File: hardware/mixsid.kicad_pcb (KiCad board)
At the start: 2 copper layers, 61 x 55.9 mm, 69 parts, among them P1 INPUT, P2 CONTROL, P4 SOCKET LEFT, P5 OUTPUT, P6 SOCKET RIGHT, Q1 BC547, Q2 BC547, U1 GAL16V8, U2 SID2, U3 7812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

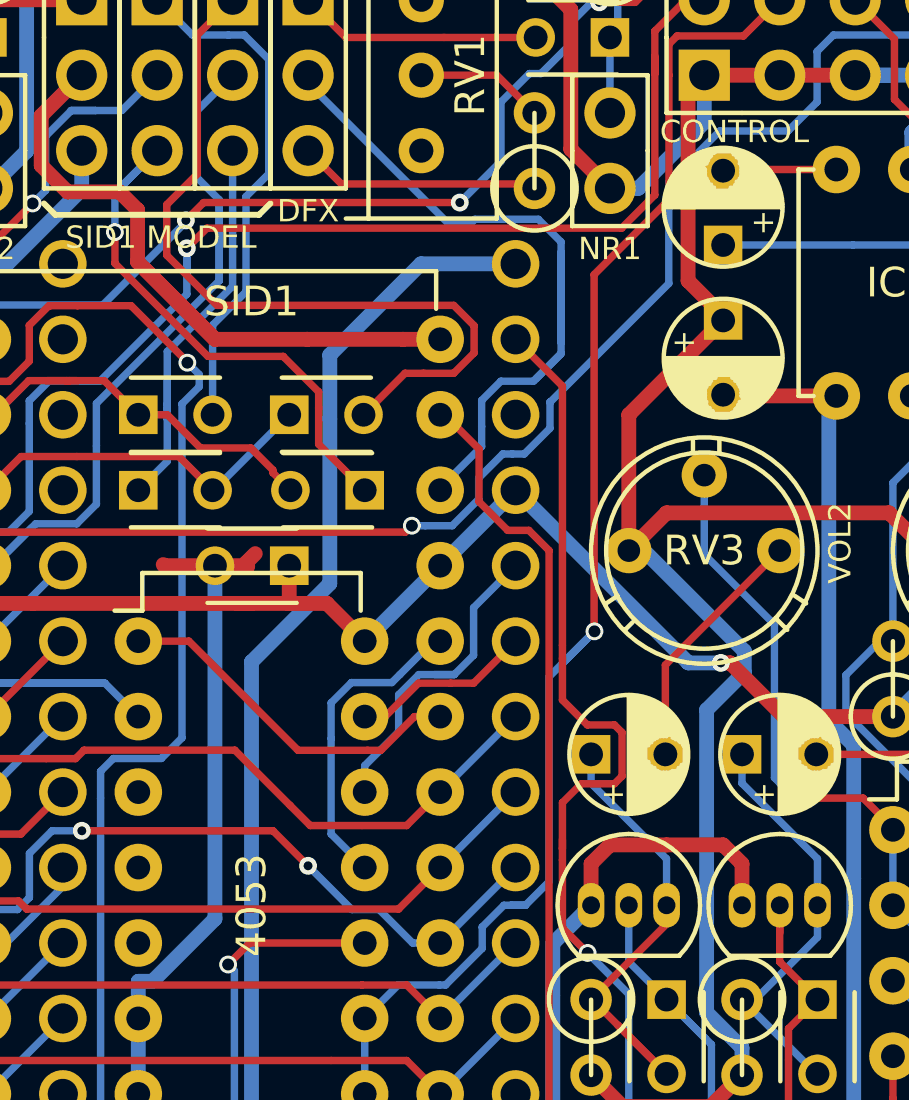
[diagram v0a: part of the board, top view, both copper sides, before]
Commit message: Hardware: Added pin header to access raw audio out as well
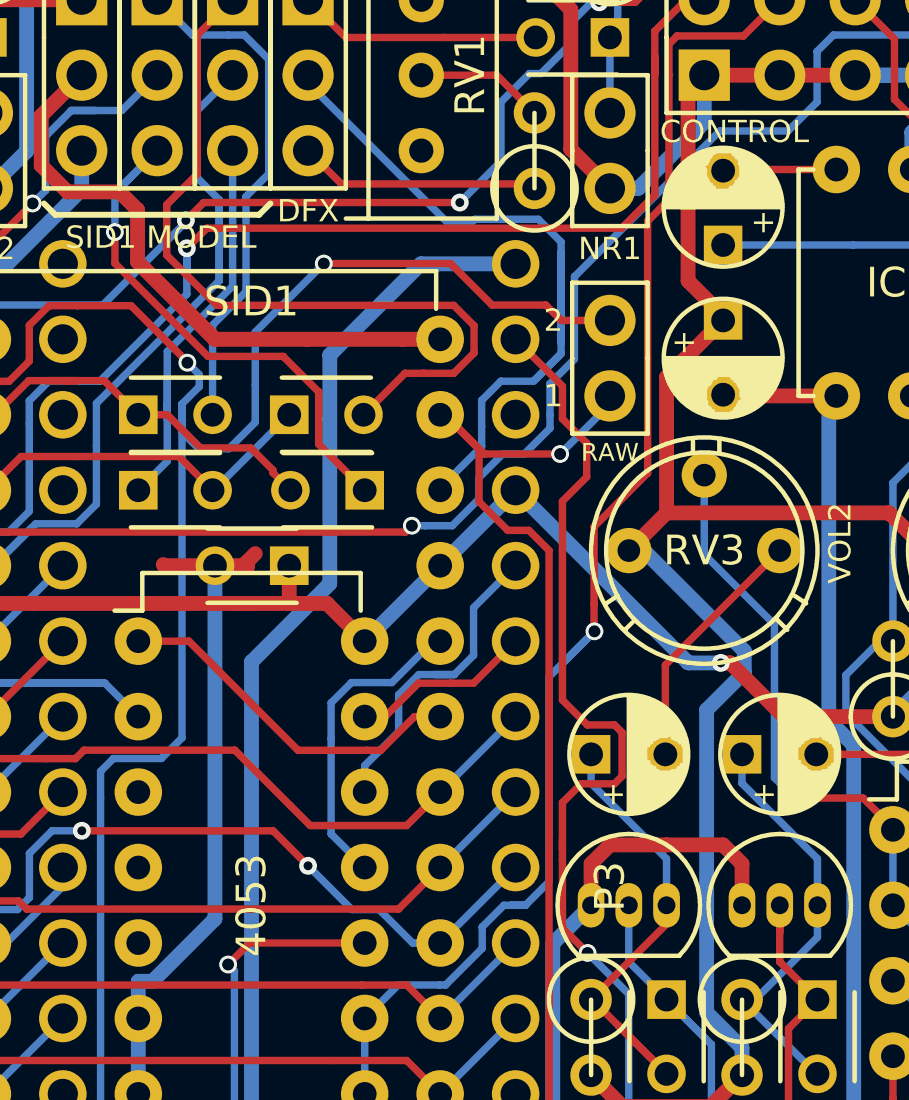
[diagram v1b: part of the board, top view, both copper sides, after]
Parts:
- added P3: RAW, Pinheaders:Pin_Header_Straight_1x02, F.Cu at (169.5, 80.6)
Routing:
- net /S2OUT: track 68.2 -> 88.9 mm, vias 2 -> 3
- net /S1OUT: track 40.4 -> 47.7 mm, vias 0 -> 1
- net GND: track 299.8 -> 298.0 mm
- net /MONO_OUT: track 43.8 -> 44.5 mm
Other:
- board text added: "1"
- board text added: "2"
- board text added: "RAW"

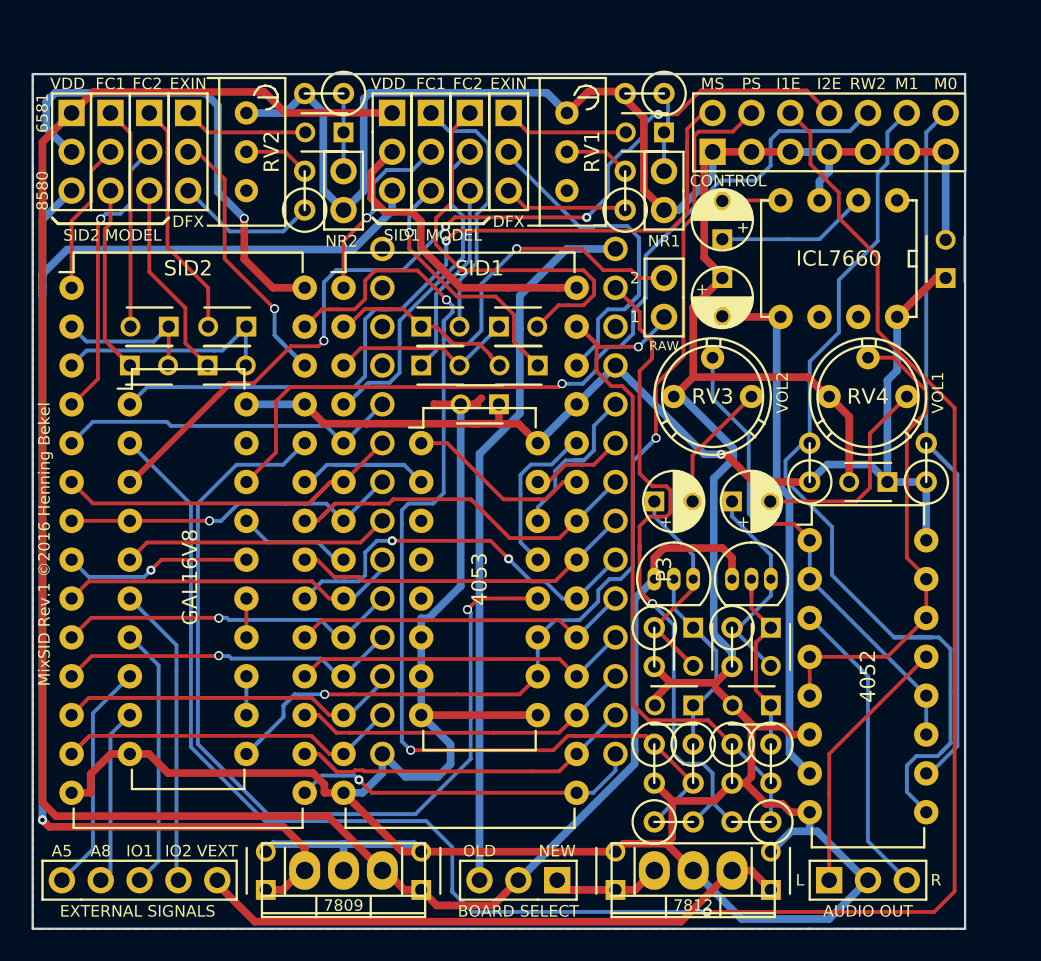
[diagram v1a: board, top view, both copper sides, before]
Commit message: Hardware: Improved thermal release at ground connections
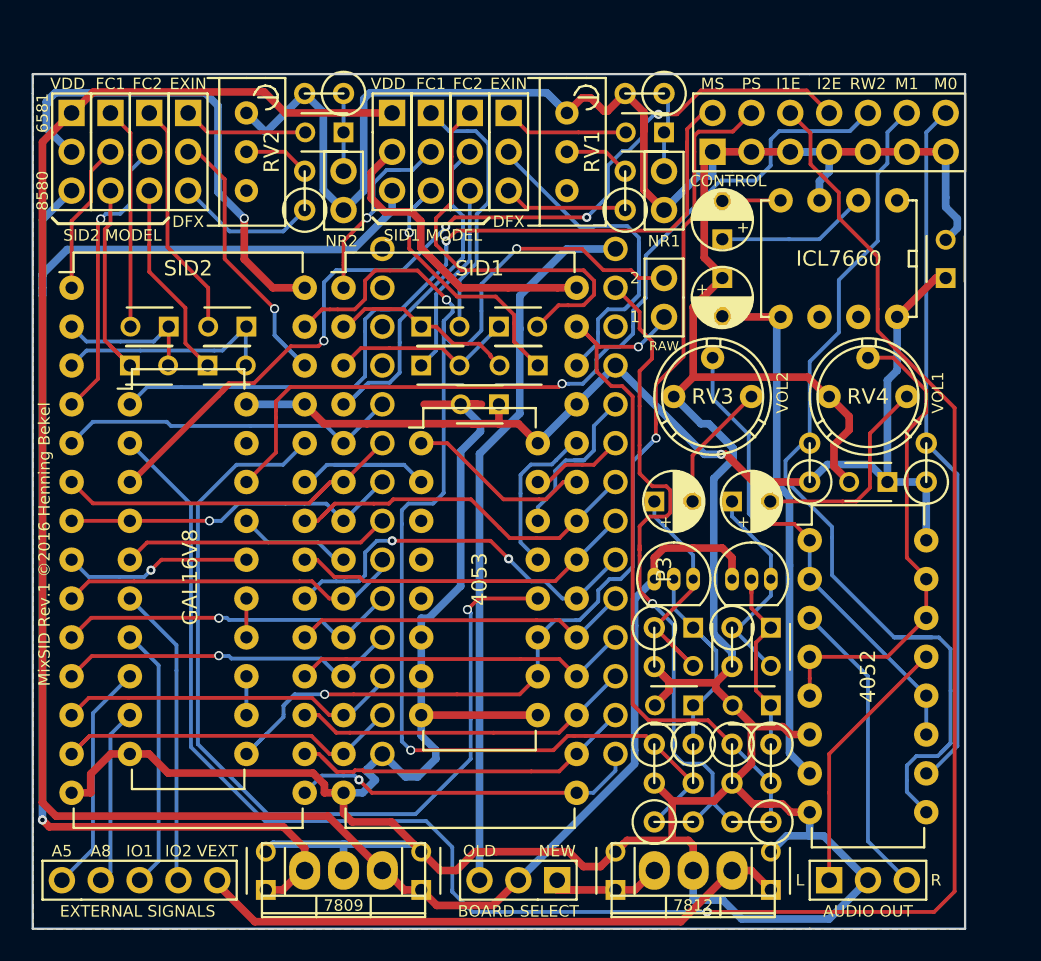
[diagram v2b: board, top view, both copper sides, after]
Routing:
- net GND: track 298.0 -> 312.2 mm

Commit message: Hardware: Improved routing and silkscreen
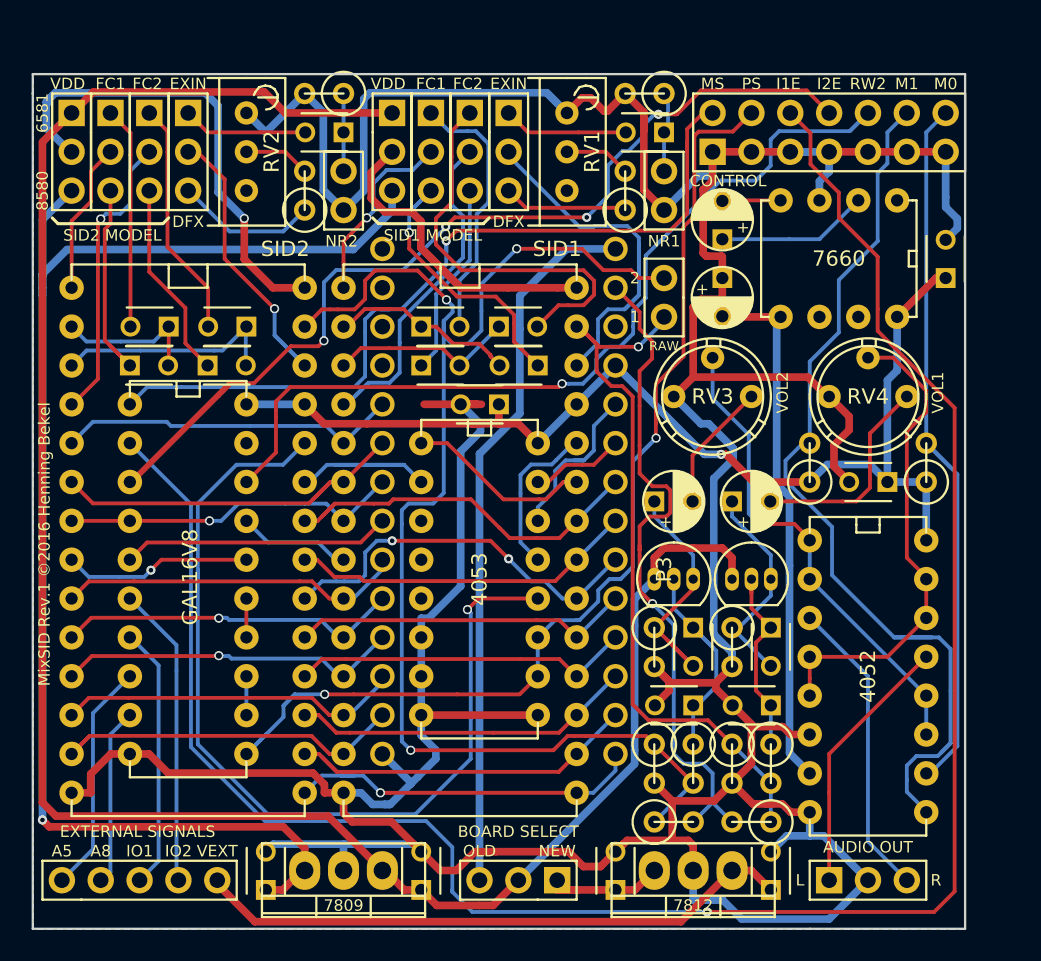
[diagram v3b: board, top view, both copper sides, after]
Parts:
- U1: footprint Housings_DIP:DIP-20_W7.62mm -> Pinheaders:DIP-20_W7.62mm
- U2, U5: footprint Housings_DIP:DIP-28_W15.24mm -> Pinheaders:DIP-28_W15.24mm
- U6, U7: footprint Housings_DIP:DIP-16_W7.62mm -> Pinheaders:DIP-16_W7.62mm
- U8: value ICL7660 -> 7660
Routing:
- net GND: track 312.2 -> 315.5 mm
- net /D0: track 22.9 -> 23.9 mm

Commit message: Hardware: Added -5V test point, improved silkscreen
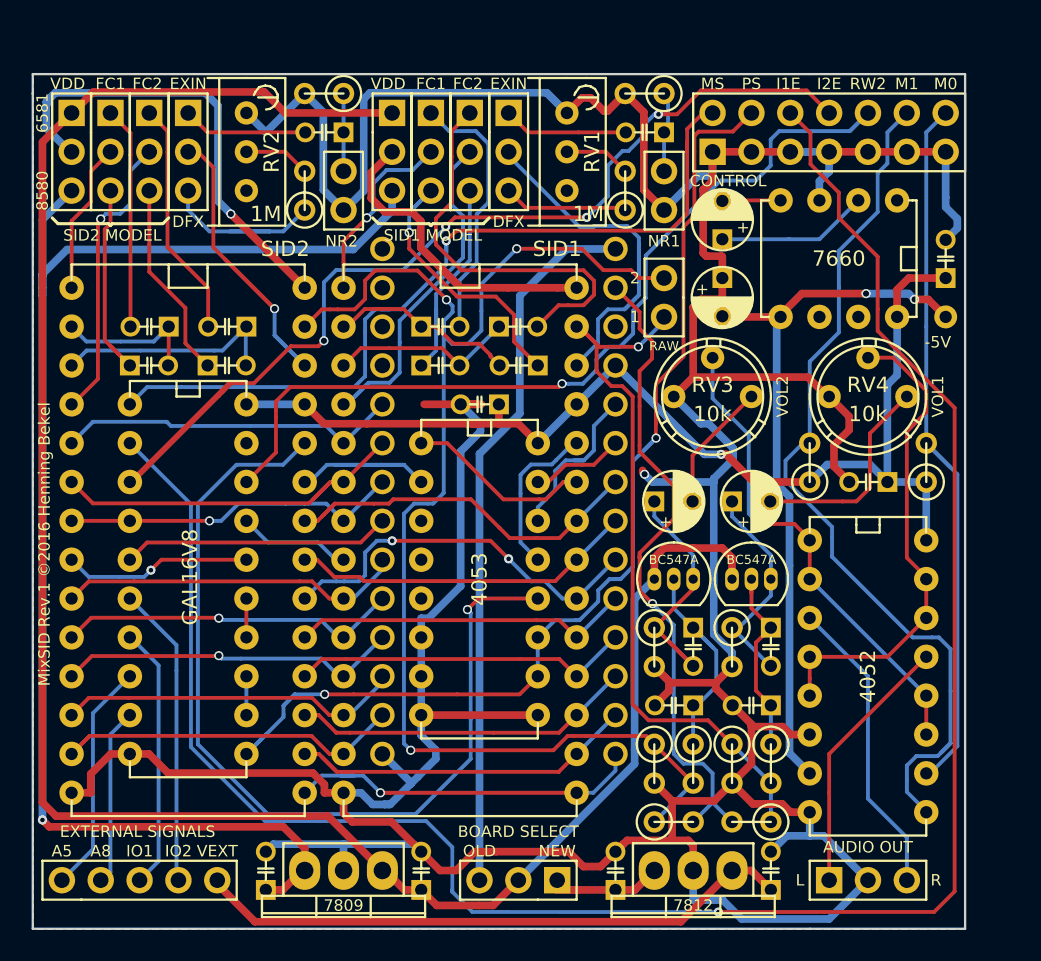
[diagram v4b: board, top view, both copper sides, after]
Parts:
- added P7: -5V, Measurement_Points:Measurement_Point_Round-TH_Small, F.Cu at (188.0, 83.2)
- C1, C10, C11, C12, C13, C14, C15, C16, C2, C20, C21, C23, C24, C25, C3, C4, C5, C6, C7, C8, C9: footprint Capacitors_ThroughHole:C_Disc_D3_P2.5 -> Pinheaders:C_Disc_D3_P2.5
- R1, R10, R11, R12, R13, R14, R2, R3, R4, R5, R6, R7, R8, R9: footprint Discret:R1 -> Pinheaders:R1
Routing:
- net /VEE: track 34.7 -> 48.5 mm, vias 0 -> 2
- net /S2IN: track 20.3 -> 25.5 mm
- net GND: track 315.5 -> 320.5 mm, vias 0 -> 1
- net Net-(JP8-Pad3): track 9.30 -> 12.7 mm
- net /M1: track 61.3 -> 58.2 mm
- net VCC: track 72.9 -> 74.6 mm
- net /PWR2: track 32.6 -> 31.4 mm
- net /MONO_OUT: track 44.5 -> 43.3 mm
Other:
- board text added: "-5V"
- board text added: "BC547A"

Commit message: Hardware: Improved silkscreen
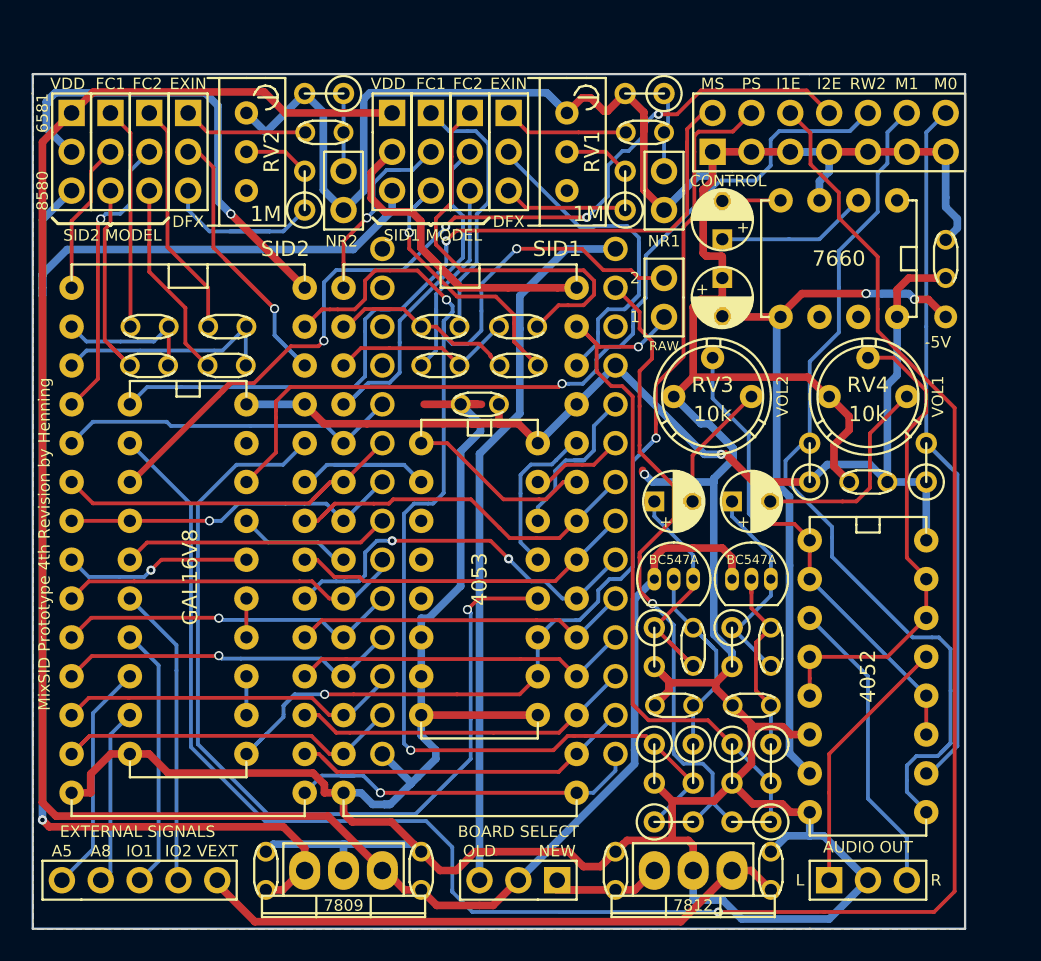
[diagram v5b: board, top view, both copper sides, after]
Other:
- board text added: "MixSID Prototype 4th Revision by Henning"
- board text removed: "MixSID Rev.1 ©2016 Henning Bekel"

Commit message: Hardware: Improved component placement, cap orientation for 7660
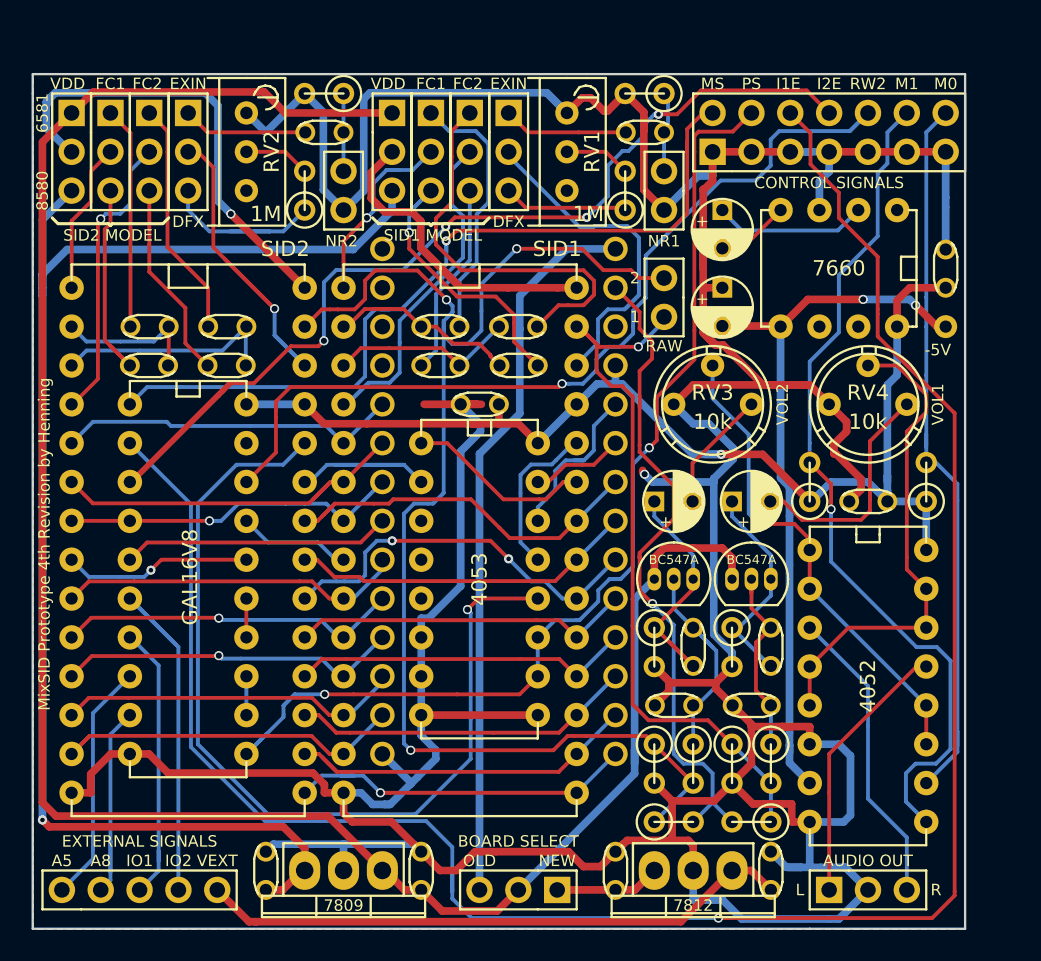
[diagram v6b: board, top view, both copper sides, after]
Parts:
- moved C17 1.91 mm to (173.4, 76.2), turned to 270 degrees
- moved R7 1.27 mm to (186.7, 94.0)
- moved R8 1.27 mm to (179.1, 94.0)
- moved C25 1.27 mm to (184.2, 95.2)
- moved C18 0.64 mm to (173.4, 81.3)
- moved C23 0.64 mm to (188.0, 81.3)
- moved JP4 0.64 mm to (162.6, 120.7)
- moved P1 0.64 mm to (130.2, 120.7)
- moved P5 0.64 mm to (180.3, 120.7)
- moved U8 0.64 mm to (184.8, 76.2)
- moved P7 0.63 mm to (188.0, 83.8)
- moved U6 0.63 mm to (179.1, 98.4)
- moved RV3 0.51 mm to (170.2, 88.9)
- moved RV4 0.51 mm to (180.3, 88.9)
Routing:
- net GND: track 320.5 -> 343.1 mm
- net /~IO2: track 19.8 -> 24.7 mm
- net /A8: track 11.8 -> 14.4 mm
- net Net-(C22-Pad2): track 14.2 -> 16.7 mm
- net /M1: track 58.2 -> 55.7 mm, vias 0 -> 1
- net VCC: track 74.6 -> 76.7 mm
- net /~IO1EN: track 133.5 -> 135.7 mm
- net /+12V: track 136.9 -> 138.4 mm
- net /PS: track 71.8 -> 70.2 mm
- net /PWR: track 8.19 -> 6.88 mm
- net /VEE: track 48.5 -> 47.2 mm
- net Net-(C17-Pad2): track 3.83 -> 4.85 mm
- net /D0: track 23.9 -> 23.2 mm
- net /LEFT_OUT: track 17.4 -> 18.0 mm
- net Net-(C19-Pad2): track 8.45 -> 7.94 mm
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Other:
- board text added: "CONTROL SIGNALS"
- board text removed: "CONTROL"
